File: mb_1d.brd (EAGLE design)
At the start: 100 x 80 mm, 59 parts, among them CON1 1013279X_AMPHENOL_2X25, CON2 1013279X_AMPHENOL_2X25, U1 TPS61040, U10 TPS610981, U2 MAX5394, U3 TPS61040, U4 74HC4050, U5 RFD77101, U6 MAX5394, U7 MAX5026EUT+T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

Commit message: Routed Simblee
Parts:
- moved U$2 145.8 mm to (68.8, 75.7)
- moved C17 134.9 mm to (62.2, 69.1)
- moved D6 134.1 mm to (78.5, 71.1)
- moved D5 133.6 mm to (81.8, 71.1)
- moved D4 130.4 mm to (81.8, 73.2), turned to 180 degrees
- moved U7 128.7 mm to (68.6, 72.4)
- moved C12 126.9 mm to (77.7, 75.2), turned to 270 degrees
- moved C10 124.4 mm to (82.8, 75.2), turned to 270 degrees
- moved C11 124.4 mm to (79.0, 75.2), turned to 90 degrees
- moved D3 123.5 mm to (78.5, 73.2), turned to 180 degrees
- moved R11 112.4 mm to (75.2, 75.2), turned to 90 degrees
- moved C9 112.1 mm to (73.9, 75.2), turned to 90 degrees
- moved R13 111.5 mm to (70.2, 69.9), turned to 180 degrees
- moved U9 111.4 mm to (55.0, 55.3), turned to 270 degrees
- moved R12 111.2 mm to (72.5, 69.9)
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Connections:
- net CLK_CP: now also U5.17; no longer U5.32
- net RSTB_M: now also U5.18; no longer U5.31
- net SS_POT1: now also U5.14; no longer U5.26
- net SS_POT2: now also U5.15; no longer U5.27
- net SS_POT3: now also U5.16; no longer U5.28
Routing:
- net GND: track 0.00 -> 46.5 mm, vias 0 -> 6
- net SDI_LS: track 0.00 -> 39.8 mm, vias 0 -> 2
- net CLK_CP: track 0.00 -> 35.5 mm, vias 0 -> 2
- net SCK_LS: track 0.00 -> 33.2 mm, vias 0 -> 2
- net VDD: track 0.00 -> 32.3 mm, vias 0 -> 4
- net RSTB_M: track 0.00 -> 31.1 mm, vias 0 -> 2
- net MISO: track 0.00 -> 28.6 mm, vias 0 -> 2
- net TMODE_M: track 0.00 -> 23.0 mm
- net REF_CLK: track 0.00 -> 22.4 mm, vias 0 -> 2
- net HF_M: track 0.00 -> 22.0 mm
- net DLL_START_M: track 0.00 -> 21.3 mm
- net OUT16_BUF: track 0.00 -> 20.4 mm, vias 0 -> 2
- net REF_CLK_BUF: track 0.00 -> 18.1 mm, vias 0 -> 2
- net DLL_SAMP_M: track 0.00 -> 17.6 mm
- net DLL_EN_M: track 0.00 -> 16.8 mm
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
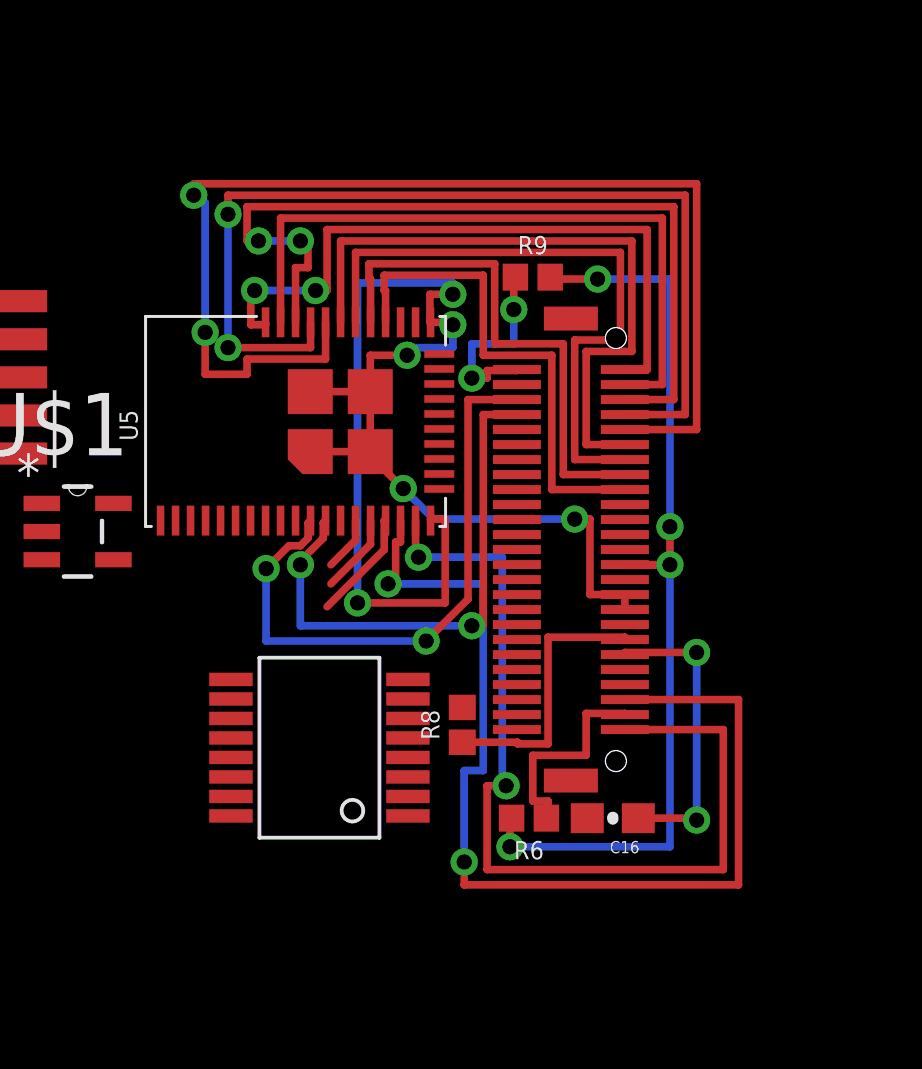
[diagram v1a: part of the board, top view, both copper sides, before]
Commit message: Updated trace properties
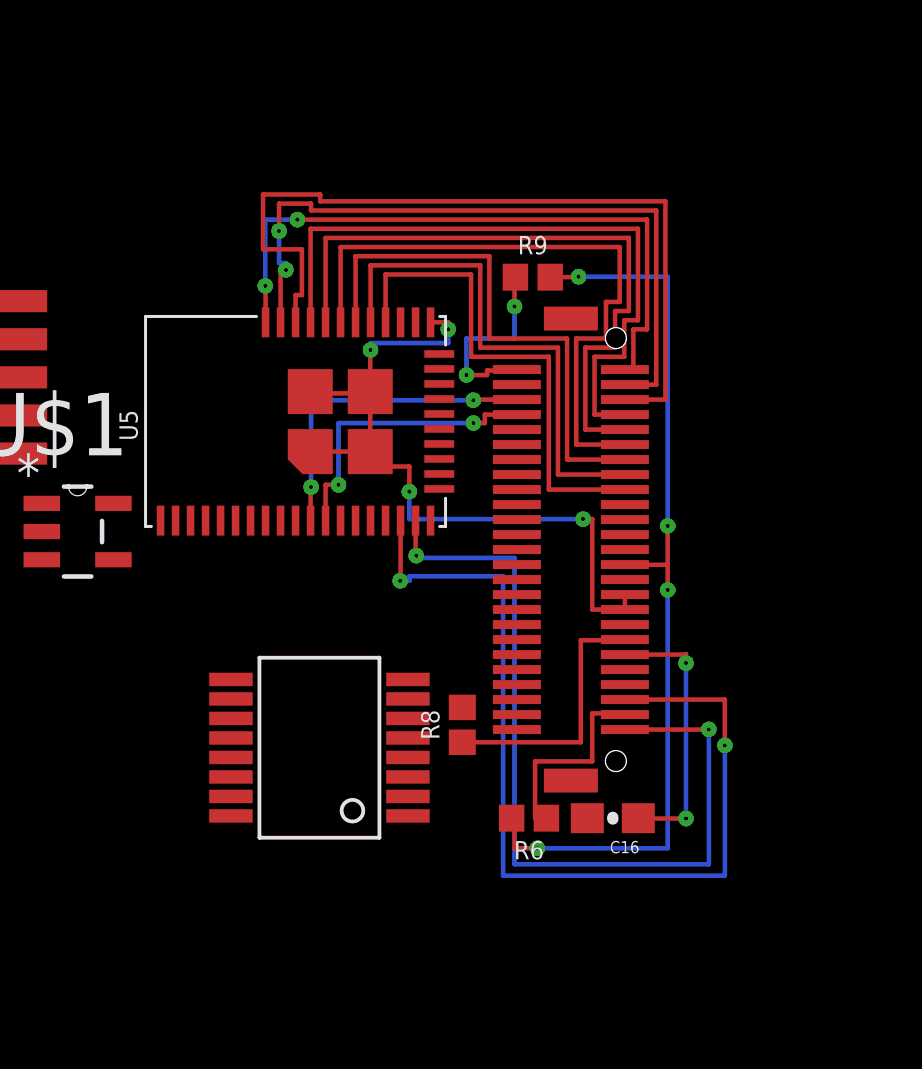
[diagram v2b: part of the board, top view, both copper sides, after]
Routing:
- net GND: track 46.5 -> 26.8 mm, vias 6 -> 4
- net SDI_LS: track 39.8 -> 22.1 mm, vias 2 -> 0
- net SCK_LS: track 33.2 -> 22.7 mm, vias 2 -> 0
- net OUT16_BUF: track 20.4 -> 10.9 mm
- net REF_CLK_BUF: track 18.1 -> 9.91 mm
- net SS_POT3: track 3.70 -> 0.00 mm
- net CLK_CP: track 35.5 -> 32.2 mm
- net DLL_START_M: track 21.3 -> 18.0 mm
- net SS_POT2: track 2.66 -> 0.00 mm
- net RSTB_M: track 31.1 -> 28.5 mm
- net SS_POT1: track 1.81 -> 0.00 mm
- net VDD: track 32.3 -> 30.6 mm
- net MISO: track 28.6 -> 27.4 mm, vias 2 -> 0
- net TMODE_M: track 23.0 -> 24.0 mm, vias 0 -> 2
- net MVDD: track 10.1 -> 9.12 mm
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
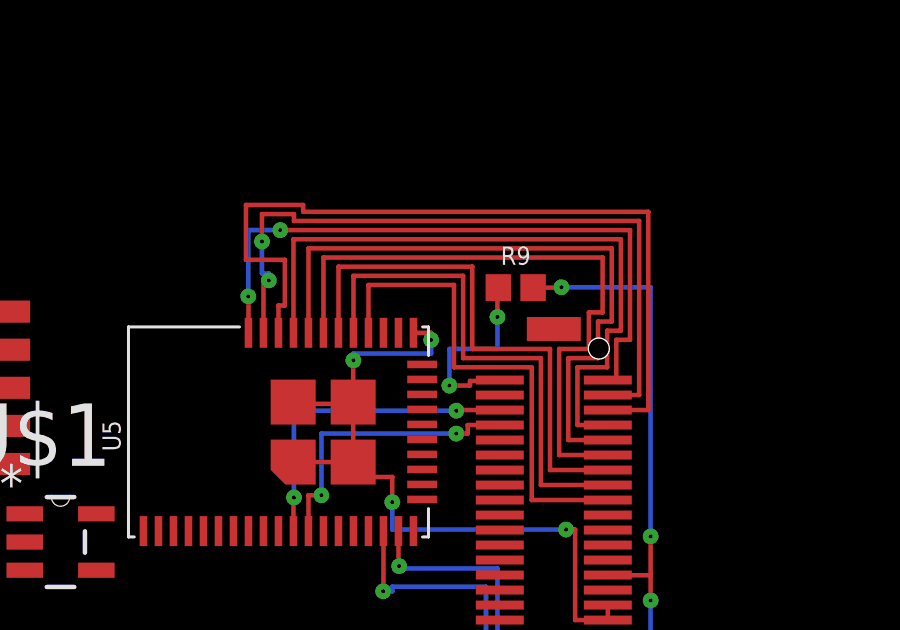
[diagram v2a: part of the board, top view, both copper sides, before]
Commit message: Updated Simblee routes
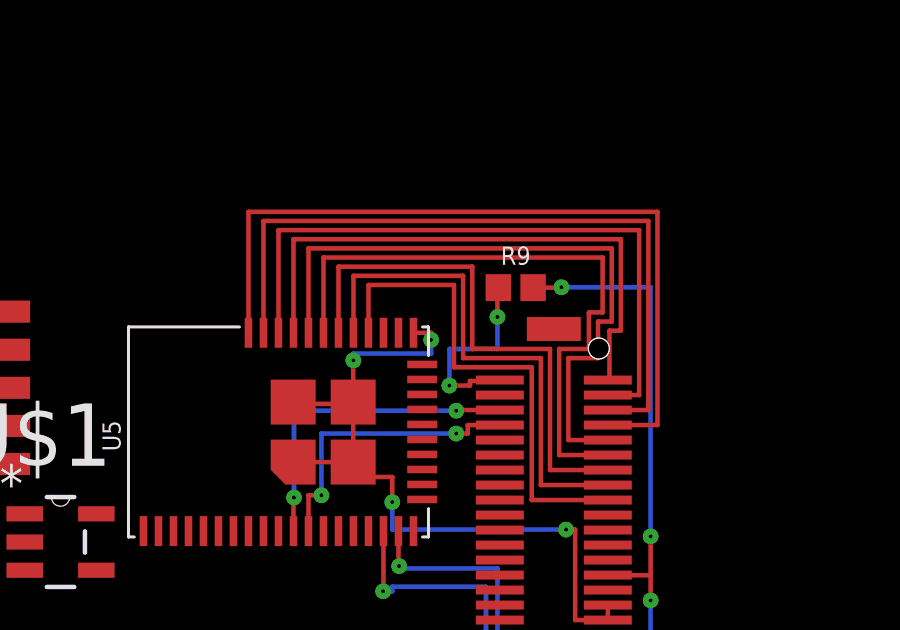
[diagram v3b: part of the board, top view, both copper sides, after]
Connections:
- net MISO: now also U5.40; no longer U5.39
- net REF_CLK: now also U5.38; no longer U5.41
- net SCK_LS: now also U5.41; no longer U5.38
- net TMODE_M: now also U5.39; no longer U5.40
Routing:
- net SCK_LS: track 22.7 -> 26.4 mm
- net MISO: track 27.4 -> 24.2 mm
- net REF_CLK: track 21.9 -> 19.2 mm, vias 2 -> 0
- net TMODE_M: track 24.0 -> 22.0 mm, vias 2 -> 0
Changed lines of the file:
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@@
 <signal name="MISO">
 <contactref element="CON2" pad="48"/>
-<contactref element="U5" pad="39"/>
+<contactref element="U5" pad="40"/>
 <wire x1="75.46" y1="51.99" x2="76.8096" y2="51.99" width="0.1524" layer="1"/>
-<wire x1="76.8096" y1="51.99" x2="76.8096" y2="58.5978" width="0.1524" layer="1"/>
-<wire x1="76.8096" y1="58.5978" x2="65.3034" y2="58.5978" width="0.1524" layer="1"/>
-<wire x1="65.3034" y1="58.5978" x2="65.3034" y2="58.8264" width="0.1524" layer="1"/>
-<wire x1="65.3034" y1="58.8264" x2="63.3984" y2="58.8264" width="0.1524" layer="1"/>
-<wire x1="63.3984" y1="58.8264" x2="63.3984" y2="56.9976" width="0.1524" layer="1"/>
-<wire x1="63.3984" y1="56.9976" x2="64.6938" y2="56.9976" width="0.1524" layer="1"/>
-<wire x1="64.6938" y1="56.9976" x2="64.6938" y2="55.4736" width="0.1524" layer="1"/>
-<wire x1="64.6938" y1="55.4736" x2="64.4821" y2="55.4736" width="0.1524" layer="1"/>
-<wire x1="64.4821" y1="55.4736" x2="64.4821" y2="54.5652" width="0.1524" layer="1"/>
+<wire x1="76.8096" y1="51.99" x2="76.8096" y2="58.293" width="0.1524" layer="1"/>
+<wire x1="76.8096" y1="58.293" x2="63.9821" y2="58.293" width="0.1524" layer="1"/>
+<wire x1="63.9821" y1="58.293" x2="63.9821" y2="54.5652" width="0.1524" layer="1"/>
 </signal>
 <signal name="N$1">
@@
 <signal name="REF_CLK">
 <contactref element="CON2" pad="50"/>
-<contactref element="U5" pad="41"/>
 <contactref element="U9" pad="3"/>
-<wire x1="51.1037" y1="52.7304" x2="63.4821" y2="54.5652" width="0" layer="19" extent="1-1"/>
-<wire x1="75.46" y1="52.99" x2="75.7428" y2="52.99" width="0.1524" layer="1"/>
-<wire x1="75.7428" y1="52.99" x2="75.7428" y2="54.3306" width="0.1524" layer="1"/>
-<wire x1="75.7428" y1="54.3306" x2="76.2" y2="54.3306" width="0.1524" layer="1"/>
-<wire x1="76.2" y1="54.3306" x2="76.2" y2="57.9882" width="0.1524" layer="1"/>
-<wire x1="76.2" y1="57.9882" x2="64.5414" y2="57.9882" width="0.1524" layer="1"/>
-<via x="64.5414" y="57.9882" extent="1-16" drill="0.127" diameter="0.381"/>
-<wire x1="64.5414" y1="57.9882" x2="63.4746" y2="57.9882" width="0.1524" layer="16"/>
-<wire x1="63.4746" y1="57.9882" x2="63.4746" y2="55.7784" width="0.1524" layer="16"/>
-<via x="63.4746" y="55.7784" extent="1-16" drill="0.127" diameter="0.381"/>
-<wire x1="63.4746" y1="55.7784" x2="63.4821" y2="55.7784" width="0.1524" layer="1"/>
-<wire x1="63.4821" y1="55.7784" x2="63.4821" y2="54.5652" width="0.1524" layer="1"/>
+<contactref element="U5" pad="38"/>
+<wire x1="51.1037" y1="52.7304" x2="64.9821" y2="54.5652" width="0" layer="19" extent="1-1"/>
+<wire x1="75.46" y1="52.99" x2="75.5142" y2="52.99" width="0.1524" layer="1"/>
+<wire x1="75.5142" y1="52.99" x2="75.5142" y2="54.6354" width="0.1524" layer="1"/>
+<wire x1="75.5142" y1="54.6354" x2="75.8952" y2="54.6354" width="0.1524" layer="1"/>
+<wire x1="75.8952" y1="54.6354" x2="75.8952" y2="57.6834" width="0.1524" layer="1"/>
+<wire x1="75.8952" y1="57.6834" x2="64.9821" y2="57.6834" width="0.1524" layer="1"/>
+<wire x1="64.9821" y1="57.6834" x2="64.9821" y2="54.5652" width="0.1524" layer="1"/>
 </signal>
 <signal name="REF_CLK_BUF">
@@
 <signal name="TMODE_M">
 <contactref element="CON2" pad="49"/>
-<contactref element="U5" pad="40"/>
+<contactref element="U5" pad="39"/>
 <wire x1="75.46" y1="52.49" x2="76.5048" y2="52.49" width="0.1524" layer="1"/>
-<wire x1="76.5048" y1="52.49" x2="76.5048" y2="58.293" width="0.1524" layer="1"/>
-<wire x1="76.5048" y1="58.293" x2="64.9986" y2="58.293" width="0.1524" layer="1"/>
-<wire x1="64.9986" y1="58.293" x2="64.9986" y2="58.5216" width="0.1524" layer="1"/>
-<wire x1="64.9986" y1="58.5216" x2="63.9318" y2="58.5216" width="0.1524" layer="1"/>
-<wire x1="63.9318" y1="58.5216" x2="63.9318" y2="57.6072" width="0.1524" layer="1"/>
-<via x="63.9318" y="57.6072" extent="1-16" drill="0.127" diameter="0.381"/>
-<wire x1="63.9318" y1="57.6072" x2="63.9318" y2="56.5404" width="0.1524" layer="16"/>
-<wire x1="63.9318" y1="56.5404" x2="64.1604" y2="56.5404" width="0.1524" layer="16"/>
-<wire x1="64.1604" y1="56.5404" x2="64.1604" y2="56.3118" width="0.1524" layer="16"/>
-<via x="64.1604" y="56.3118" extent="1-16" drill="0.127" diameter="0.381"/>
-<wire x1="64.1604" y1="56.3118" x2="63.9821" y2="56.3118" width="0.1524" layer="1"/>
-<wire x1="63.9821" y1="56.3118" x2="63.9821" y2="54.5652" width="0.1524" layer="1"/>
+<wire x1="76.5048" y1="52.49" x2="76.5048" y2="57.9882" width="0.1524" layer="1"/>
+<wire x1="76.5048" y1="57.9882" x2="64.4821" y2="57.9882" width="0.1524" layer="1"/>
+<wire x1="64.4821" y1="57.9882" x2="64.4821" y2="54.5652" width="0.1524" layer="1"/>
 </signal>
 <signal name="DLL_START_M">
@@
 <contactref element="CON2" pad="47"/>
 <contactref element="U4" pad="2"/>
-<contactref element="U5" pad="38"/>
 <contactref element="U8" pad="5"/>
 <contactref element="U6" pad="5"/>
 <contactref element="U2" pad="5"/>
+<contactref element="U5" pad="41"/>
 <wire x1="68.228" y1="38.761" x2="75.46" y2="51.49" width="0" layer="19" extent="1-1"/>
 <wire x1="48.54" y1="26.658" x2="68.228" y2="38.761" width="0" layer="19" extent="1-1"/>
 <wire x1="31.649" y1="19.8" x2="48.54" y2="26.658" width="0" layer="19" extent="1-1"/>
 <wire x1="31.4585" y1="16.1805" x2="31.649" y2="19.8" width="0" layer="19" extent="1-1"/>
-<wire x1="75.46" y1="51.49" x2="74.4474" y2="51.49" width="0.1524" layer="1"/>
-<wire x1="74.4474" y1="51.49" x2="74.4474" y2="53.4162" width="0.1524" layer="1"/>
-<wire x1="74.4474" y1="53.4162" x2="75.438" y2="53.4162" width="0.1524" layer="1"/>
-<wire x1="75.438" y1="53.4162" x2="75.438" y2="54.6354" width="0.1524" layer="1"/>
-<wire x1="75.438" y1="54.6354" x2="75.8952" y2="54.6354" width="0.1524" layer="1"/>
-<wire x1="75.8952" y1="54.6354" x2="75.8952" y2="57.6834" width="0.1524" layer="1"/>
-<wire x1="75.8952" y1="57.6834" x2="64.9821" y2="57.6834" width="0.1524" layer="1"/>
-<wire x1="64.9821" y1="57.6834" x2="64.9821" y2="54.5652" width="0.1524" layer="1"/>
+<wire x1="75.46" y1="51.49" x2="77.1144" y2="51.49" width="0.1524" layer="1"/>
+<wire x1="77.1144" y1="51.49" x2="77.1144" y2="58.5978" width="0.1524" layer="1"/>
+<wire x1="77.1144" y1="58.5978" x2="63.4821" y2="58.5978" width="0.1524" layer="1"/>
+<wire x1="63.4821" y1="58.5978" x2="63.4821" y2="54.5652" width="0.1524" layer="1"/>
 </signal>
 <signal name="HVDC">

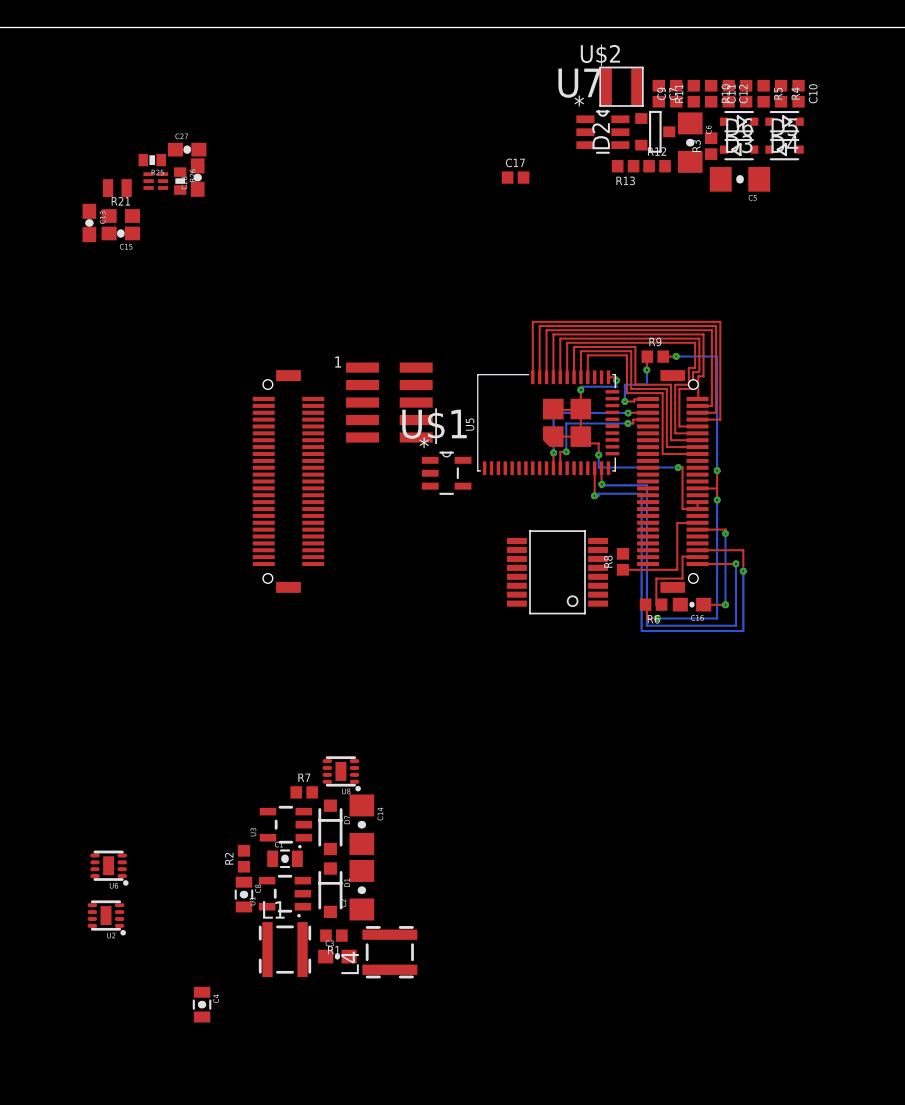
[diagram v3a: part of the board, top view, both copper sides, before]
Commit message: First version of completed routing
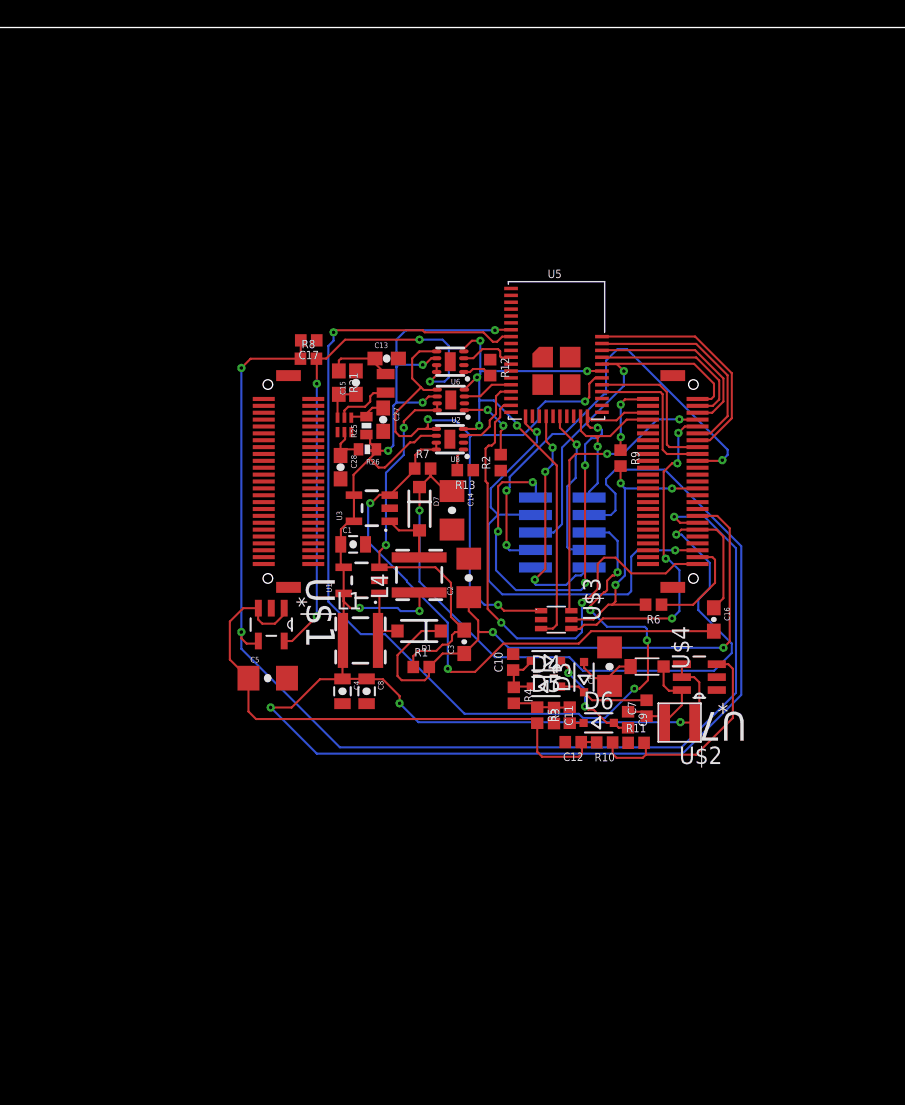
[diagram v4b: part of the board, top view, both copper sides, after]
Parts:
- removed D2: ZHCS1000, zetex:SOT-23
- removed U4: 74HC4050, ck:16-TSSOP
- added U$3: (no value), Personal:SN74AUP2G34DCKR
- added U$4: (no value), Personal:DB2J40700L
- moved C5 49.9 mm to (44.2, 32.7), turned to 0 degrees
- moved C12 48.5 mm to (66.4, 28.0), turned to 180 degrees
- moved R5 48.1 mm to (63.8, 30.0)
- moved R4 47.9 mm to (62.1, 31.4)
- moved R10 47.8 mm to (68.7, 28.0), turned to 180 degrees
- moved R11 47.4 mm to (71.0, 28.0), turned to 0 degrees
- moved C11 47.3 mm to (65.0, 30.0), turned to 270 degrees
- moved U$2 46.7 mm to (75.3, 29.5), turned to 180 degrees
- moved C10 46.2 mm to (62.1, 33.9), turned to 90 degrees
- moved C9 45.7 mm to (70.4, 29.7), turned to 270 degrees
- moved U2 45.1 mm to (57.5, 52.9)
- moved C7 44.7 mm to (71.8, 30.5), turned to 90 degrees
- moved D4 44.6 mm to (64.4, 32.1), turned to 0 degrees
- moved U6 44.3 mm to (57.5, 55.7)
- moved D6 42.9 mm to (68.3, 29.4)
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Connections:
- removed net MOSI_LS: U2.4, U4.6, U6.4, U8.4
- removed net N$3: C6.1, D2.1, D3.A
- removed net N$8: C7.1, C9.1, D2.3, U$2.2, U7.6
- new net DIODE1: C6.1, D3.A, U$4.1
- new net DIODE2: C7.1, C9.1, U$2.2, U$4.2, U7.6
- net CLK_CP: now also U5.20; no longer U5.17
- net DLL_START_M: now also U5.41; no longer U5.35
- net GND: now also U$3.2; no longer U4.8
- net HF_M: now also U5.40; no longer U5.36
- net MISO: now also U5.39; no longer U5.40
- net MOSI: now also U$3.3, U2.4, U5.36, U6.4, U8.4; no longer U4.5
- net OUT16_BUF: now also U5.29; no longer U5.11
- net REF_CLK: now also U5.37; no longer U5.38
- net REF_CLK_BUF: now also U5.28; no longer U5.12
- net SCK: now also U$3.1, U2.5, U5.35, U6.5, U8.5; no longer U4.3
- net SCK_LS: now also U$3.6; no longer U2.5, U4.2, U5.41, U6.5, U8.5
- net SDI_LS: now also U$3.4; no longer U4.4, U5.37
- net SS_POT1: now also U5.11; no longer U5.14
- net TMODE_M: now also U5.38; no longer U5.39
- net VDD: now also U$3.5; no longer U4.1
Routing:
- net 3.3V: track 0.00 -> 162.3 mm, vias 0 -> 9
- net RESET: track 0.00 -> 77.8 mm, vias 0 -> 5
- net HVDC: track 8.84 -> 86.7 mm, vias 0 -> 3
- net MVDD: track 9.12 -> 57.0 mm
- net SCK: track 0.00 -> 46.8 mm, vias 0 -> 3
- net HVDD: track 0.15 -> 46.3 mm, vias 0 -> 2
- net FB_POT1: track 0.00 -> 42.7 mm, vias 0 -> 2
- net 50V: track 0.00 -> 42.1 mm
- net MOSI: track 0.00 -> 39.9 mm, vias 0 -> 5
- net ADJ: track 0.00 -> 37.4 mm, vias 0 -> 4
- net TX_EN_M: track 0.00 -> 34.3 mm, vias 0 -> 3
- net FB_POT: track 0.00 -> 29.6 mm, vias 0 -> 2
- net GND: track 26.8 -> 0.00 mm, vias 4 -> 0
- net OUT16_BUF: track 10.9 -> 36.0 mm, vias 2 -> 5
- net AIN2: track 0.00 -> 17.4 mm, vias 0 -> 3
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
